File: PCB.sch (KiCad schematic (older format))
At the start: 33 parts

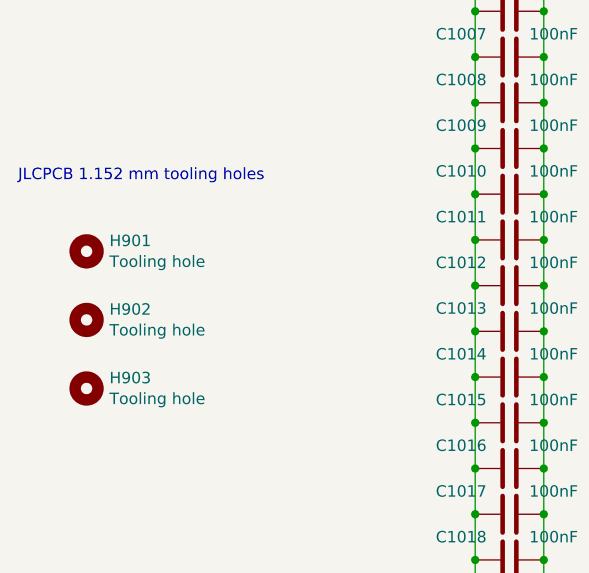
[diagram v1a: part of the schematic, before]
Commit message: Remove tooling holes from the PCB itself
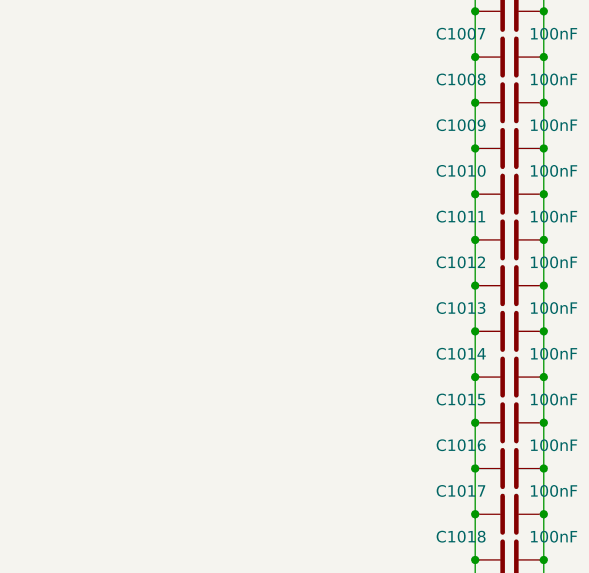
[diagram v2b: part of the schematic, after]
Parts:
- removed H901, H902, H903: Tooling hole, SH-ESP32:JlcpcbToolingHole, symbol Mechanical:MountingHole
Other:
- note removed: "JLCPCB 1.152 mm tooling holes"
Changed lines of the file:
@@
 	4700 3250 4700 3050
 Connection ~ 4400 3250
-$Comp
-L Mechanical:MountingHole H901
-U 1 1 60160A7D
-P 1900 3900
-F 0 "H901" H 2000 3946 50  0000 L CNN
-F 1 "Tooling hole" H 2000 3855 50  0000 L CNN
-F 2 "SH-ESP32:JlcpcbToolingHole" H 1900 3900 50  0001 C CNN
-F 3 "~" H 1900 3900 50  0001 C CNN
-	1    1900 3900
-	1    0    0    -1
-$EndComp
-$Comp
-L Mechanical:MountingHole H902
-U 1 1 601616D4
-P 1900 4200
-F 0 "H902" H 2000 4246 50  0000 L CNN
-F 1 "Tooling hole" H 2000 4155 50  0000 L CNN
-F 2 "SH-ESP32:JlcpcbToolingHole" H 1900 4200 50  0001 C CNN
-F 3 "~" H 1900 4200 50  0001 C CNN
-	1    1900 4200
-	1    0    0    -1
-$EndComp
-$Comp
-L Mechanical:MountingHole H903
-U 1 1 6016213C
-P 1900 4500
-F 0 "H903" H 2000 4546 50  0000 L CNN
-F 1 "Tooling hole" H 2000 4455 50  0000 L CNN
-F 2 "SH-ESP32:JlcpcbToolingHole" H 1900 4500 50  0001 C CNN
-F 3 "~" H 1900 4500 50  0001 C CNN
-	1    1900 4500
-	1    0    0    -1
-$EndComp
-Text Notes 1600 3600 0    50   ~ 0
-JLCPCB 1.152 mm tooling holes
 $EndSCHEMATC
